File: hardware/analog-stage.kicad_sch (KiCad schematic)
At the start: 4 parts, among them U701 AD9834, U702 OPA695, U703 THS3491, U704 TS5A3159ADCK

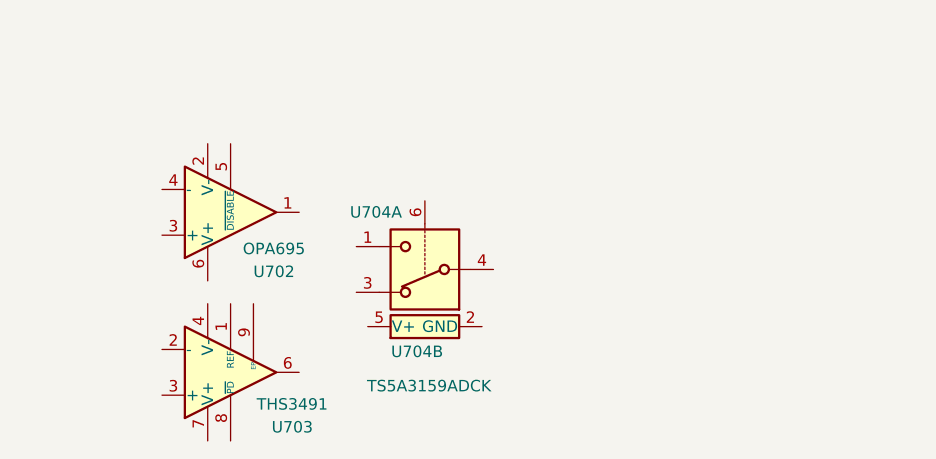
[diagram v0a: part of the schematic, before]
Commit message: Begin analog
Created LTspice simulation for square wave AC coupling.
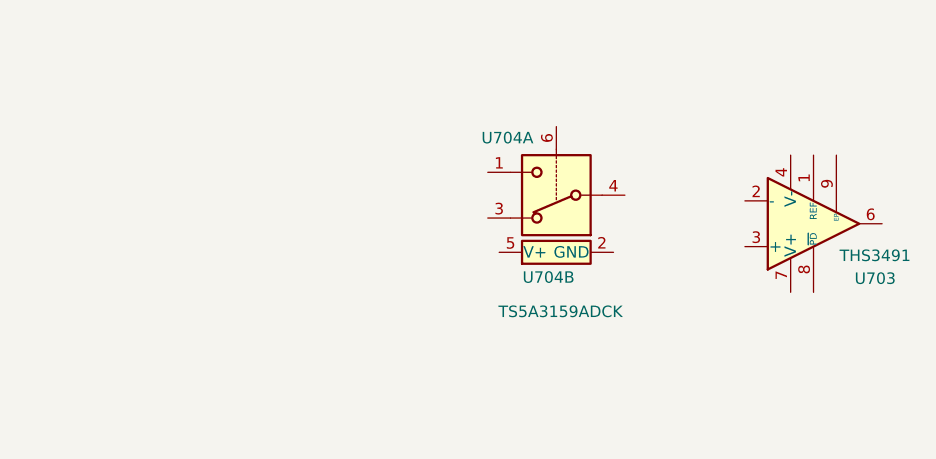
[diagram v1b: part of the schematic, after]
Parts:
- removed U702: OPA695, Package_TO_SOT_SMD:SOT-23-6, symbol carrier-wave:OPA695
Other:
- moved on the sheet: U703, U704A, U704B

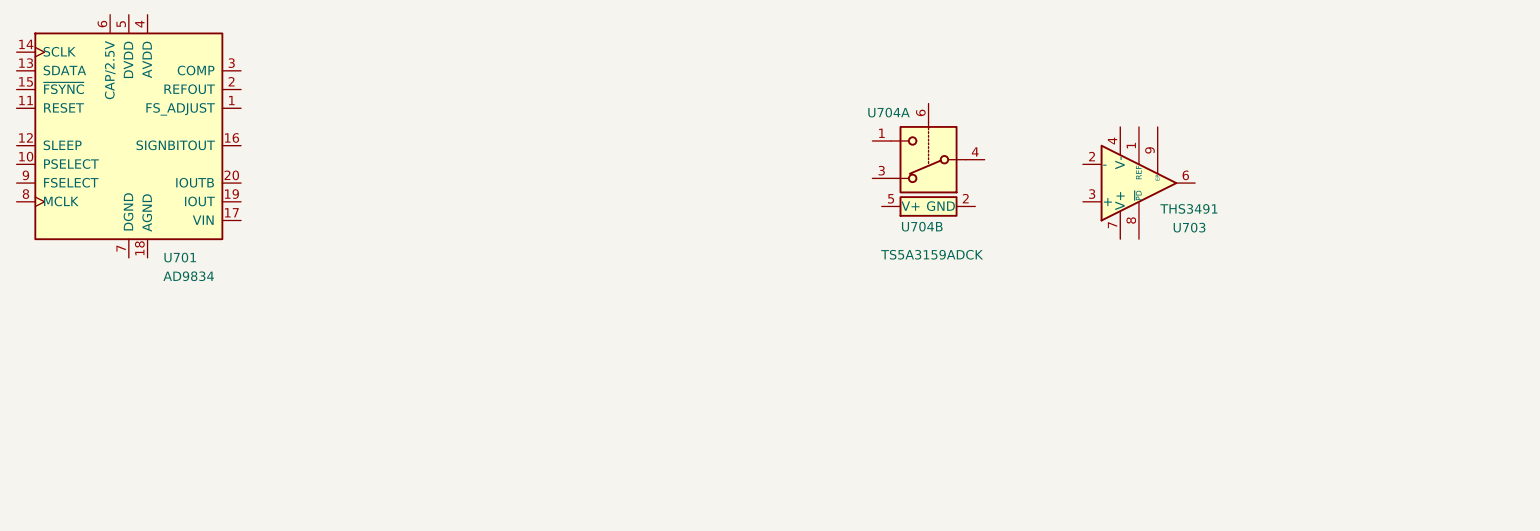
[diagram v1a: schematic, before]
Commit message: Place analog components
Proposed analog amp components in schematic
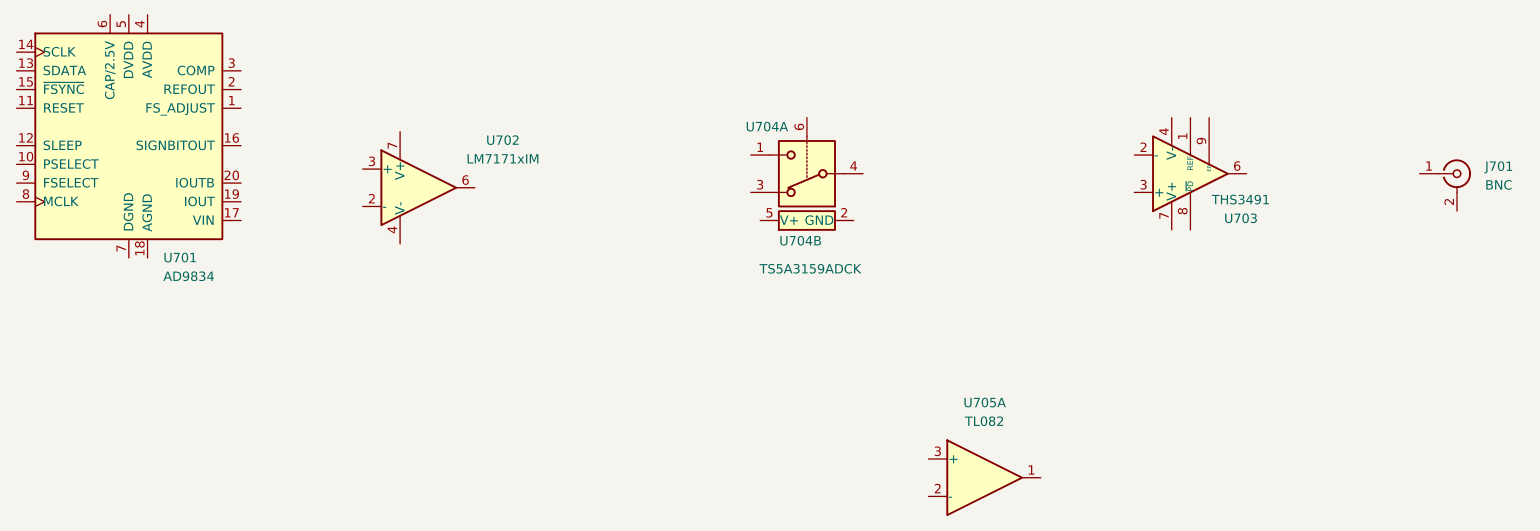
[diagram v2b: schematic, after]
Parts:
- added J701: BNC, symbol Connector:Conn_Coaxial
- added U702: LM7171xIM, Package_SO:SOIC-8_3.9x4.9mm_P1.27mm, symbol Amplifier_Operational:LM7171xIM
- added U705: TL082, Package_SO:SOIC-8_3.9x4.9mm_P1.27mm, symbol Amplifier_Operational:TL082
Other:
- moved on the sheet: U703, U704A, U704B

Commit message: Begin VGA impl
Sim and notes on adjusting to 4.5V rails for VGA.
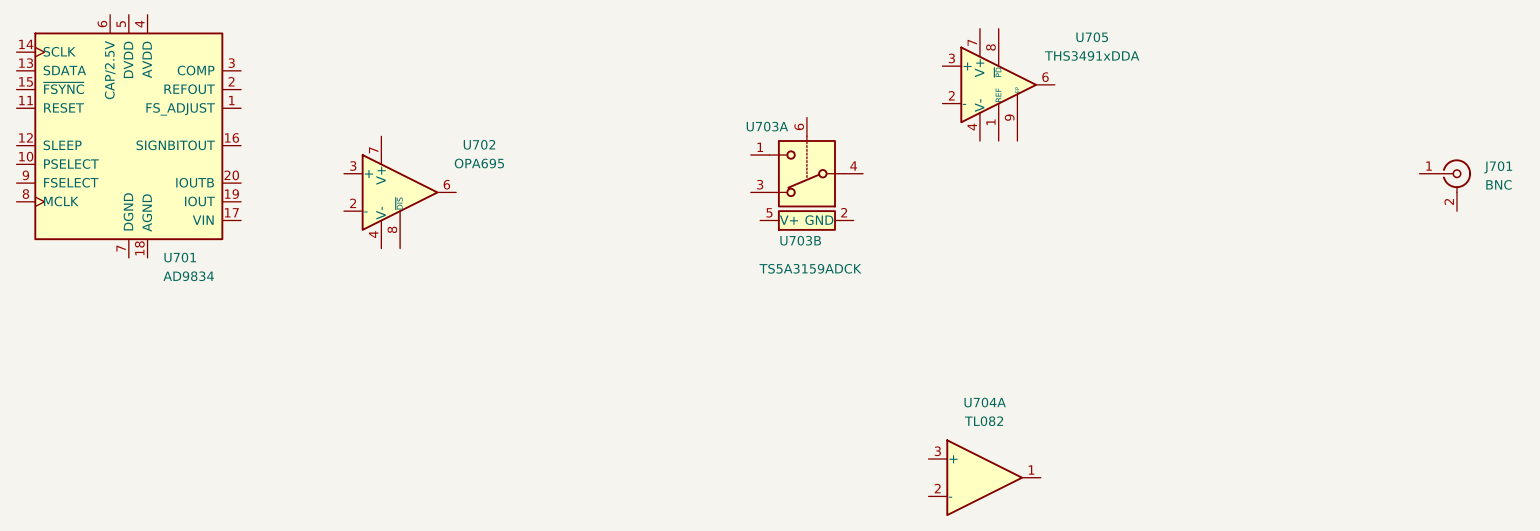
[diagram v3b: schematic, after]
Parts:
- removed U702: LM7171xIM, Package_SO:SOIC-8_3.9x4.9mm_P1.27mm, symbol Amplifier_Operational:LM7171xIM
- removed U703: THS3491, Package_SO:Texas_R-PDSO-G8_EP2.95x4.9mm_Mask2.4x3.1mm_ThermalVias, symbol Amplifier_Operational:THS3491xDDA
- added U702: OPA695, Package_SO:SOIC-8_3.9x4.9mm_P1.27mm, symbol carrier-wave:OPA695
- added U705: THS3491xDDA, Package_SO:Texas_R-PDSO-G8_EP2.95x4.9mm_Mask2.4x3.1mm_ThermalVias, symbol Amplifier_Operational:THS3491xDDA
- renumbered U704 to U703, U705 to U704
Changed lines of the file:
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@@
+	)
+	(symbol
+		(lib_id "carrier-wave:OPA695")
+		(at 97.79 97.79 0)
+		(unit 1)
+		(body_style 1)
+		(exclude_from_sim no)
+		(in_bom yes)
+		(on_board yes)
+		(in_pos_files yes)
+		(dnp no)
+		(fields_autoplaced yes)
+		(property "Reference" "U702"
+			(at 108.585 91.3698 0)
+			(show_name no)
+			(do_not_autoplace no)
+			(effects
+				(font
+					(size 1.27 1.27)
+				)
+			)
+		)
+		(property "Value" "OPA695"
+			(at 108.585 93.9098 0)
+			(show_name no)
+			(do_not_autoplace no)
+			(effects
+				(font
+					(size 1.27 1.27)
+				)
+			)
+		)
+		(property "Footprint" "Package_SO:SOIC-8_3.9x4.9mm_P1.27mm"
+			(at 100.33 104.14 0)
+			(hide yes)
+			(show_name no)
+			(do_not_autoplace no)
+			(effects
+				(font
+					(size 1.27 1.27)
+				)
+				(justify left)
+			)
+		)
+		(property "Datasheet" "https://www.ti.com/lit/ds/symlink/opa695.pdf"
+			(at 101.6 93.98 0)
+			(hide yes)
+			(show_name no)
+			(do_not_autoplace no)
+			(effects
+				(font
+					(size 1.27 1.27)
+				)
+			)
+		)
+		(property "Description" "Ultra-Wideband, Current-Feedback Operational Amplifier With Disable"
+			(at 97.79 97.79 0)
+			(hide yes)
+			(show_name no)
+			(do_not_autoplace no)
+			(effects
+				(font
+					(size 1.27 1.27)
+				)
+			)
+		)
+		(property "Part Number" " OPA695IDR"
+			(at 97.79 97.79 0)
+			(hide yes)
+			(show_name no)
+			(do_not_autoplace no)
+			(effects
+				(font
+					(size 1.27 1.27)
+				)
+			)
+		)
+		(property "Vendor URL" "https://www.digikey.com/en/products/detail/texas-instruments/OPA695IDR/1572891"
+			(at 97.79 97.79 0)
+			(hide yes)
+			(show_name no)
+			(do_not_autoplace no)
+			(effects
+				(font
+					(size 1.27 1.27)
+				)
+			)
+		)
+		(pin "5"
+		)
+		(pin "2"
+		)
+		(pin "1"
+		)
+		(pin "6"
+		)
+		(pin "4"
+		)
+		(pin "3"
+		)
+		(pin "8"
+		)
+		(pin "7"
+		)
+		(instances
+			(project "carrier-wave"
+				(path "/dc900721-a2e3-4f11-b4f2-59bb3a47422e/5675522c-b478-4fae-bc1e-6c223e44ab27"
+					(reference "U702")
+					(unit 1)
+				)
+			)
+		)
+	)
+	(symbol
+		(lib_id "Amplifier_Operational:THS3491xDDA")
+		(at 179.07 83.185 0)
+		(unit 1)
+		(body_style 1)
+		(exclude_from_sim no)
+		(in_bom yes)
+		(on_board yes)
+		(in_pos_files yes)
+		(dnp no)
+		(fields_autoplaced yes)
+		(property "Reference" "U705"
+			(at 191.77 76.7648 0)
+			(show_name no)
+			(do_not_autoplace no)
+			(effects
+				(font
+					(size 1.27 1.27)
+				)
+			)
+		)
+		(property "Value" "THS3491xDDA"
+			(at 191.77 79.3048 0)
+			(show_name no)
+			(do_not_autoplace no)
+			(effects
+				(font
+					(size 1.27 1.27)
+				)
+			)
+		)
+		(property "Footprint" "Package_SO:Texas_R-PDSO-G8_EP2.95x4.9mm_Mask2.4x3.1mm_ThermalVias"
+			(at 179.07 98.425 0)
+			(hide yes)
+			(show_name no)
+			(do_not_autoplace no)
+			(effects
+				(font
+					(size 1.27 1.27)
+				)
+			)
+		)
+		(property "Datasheet" "http://www.ti.com/lit/ds/symlink/ths3491.pdf"
+			(at 182.88 79.375 0)
+			(hide yes)
+			(show_name no)
+			(do_not_autoplace no)
+			(effects
+				(font
+					(size 1.27 1.27)
+				)
+			)
+		)
+		(property "Description" "900-MHz, 500-mA High-Power Output Current Feedback Operational Amplifier, SOIC-8"
+			(at 179.07 83.185 0)
+			(hide yes)
+			(show_name no)
+			(do_not_autoplace no)
+			(effects
+				(font
+					(size 1.27 1.27)
+				)
+			)
+		)
+		(pin "2"
+		)
+		(pin "5"
+		)
+		(pin "1"
+		)
+		(pin "6"
+		)
+		(pin "7"
+		)
+		(pin "8"
+		)
+		(pin "3"
+		)
+		(pin "9"
+		)
+		(pin "4"
+		)
+		(instances
+			(project "carrier-wave"
+				(path "/dc900721-a2e3-4f11-b4f2-59bb3a47422e/5675522c-b478-4fae-bc1e-6c223e44ab27"
+					(reference "U705")
+					(unit 1)
+				)
+			)
+		)
 	)
 	(symbol
@@
 		(in_pos_files yes)
 		(dnp no)
-		(property "Reference" "U704"
+		(property "Reference" "U703"
 			(at 150.495 88.9 0)
 			(show_name no)
@@
 			(project "carrier-wave"
 				(path "/dc900721-a2e3-4f11-b4f2-59bb3a47422e/5675522c-b478-4fae-bc1e-6c223e44ab27"
-					(reference "U704")
+					(reference "U703")
 					(unit 1)
 				)
@@
 		(dnp no)
 		(fields_autoplaced yes)
-		(property "Reference" "U705"
+		(property "Reference" "U704"
 			(at 177.165 126.365 0)
 			(show_name no)
@@
 		)
 		(property "Description" "Dual JFET-Input Operational Amplifiers, DIP-8/SOIC-8/SSOP-8"
+			(at 177.165 136.525 0)
+			(hide yes)
+			(show_name no)
+			(do_not_autoplace no)
+			(effects
+				(font
+					(size 1.27 1.27)
+				)
+			)
+		)
+		(property "Part Number" ""
+			(at 177.165 136.525 0)
+			(hide yes)
+			(show_name no)
+			(do_not_autoplace no)
+			(effects
+				(font
+					(size 1.27 1.27)
+				)
+			)
+		)
+		(property "Vendor URL" ""
 			(at 177.165 136.525 0)
 			(hide yes)
@@
 			(project "carrier-wave"
 				(path "/dc900721-a2e3-4f11-b4f2-59bb3a47422e/5675522c-b478-4fae-bc1e-6c223e44ab27"
-					(reference "U705")
-					(unit 1)
-				)
-			)
-		)
-	)
-	(symbol
-		(lib_id "Amplifier_Operational:THS3491xDDA")
-		(at 205.105 95.25 0)
-		(mirror x)
-		(unit 1)
-		(body_style 1)
-		(exclude_from_sim no)
-		(in_bom yes)
-		(on_board yes)
-		(in_pos_files yes)
-		(dnp no)
-		(property "Reference" "U703"
-			(at 211.963 101.346 0)
-			(show_name no)
-			(do_not_autoplace no)
-			(effects
-				(font
-					(size 1.27 1.27)
-				)
-			)
-		)
-		(property "Value" "THS3491"
-			(at 211.963 98.806 0)
-			(show_name no)
-			(do_not_autoplace no)
-			(effects
-				(font
-					(size 1.27 1.27)
-				)
-			)
-		)
-		(property "Footprint" "Package_SO:Texas_R-PDSO-G8_EP2.95x4.9mm_Mask2.4x3.1mm_ThermalVias"
-			(at 205.105 80.01 0)
-			(hide yes)
-			(show_name no)
-			(do_not_autoplace no)
-			(effects
-				(font
-					(size 1.27 1.27)
-				)
-			)
-		)
-		(property "Datasheet" "http://www.ti.com/lit/ds/symlink/ths3491.pdf"
-			(at 208.915 99.06 0)
-			(hide yes)
-			(show_name no)
-			(do_not_autoplace no)
-			(effects
-				(font
-					(size 1.27 1.27)
-				)
-			)
-		)
-		(property "Description" "900-MHz, 500-mA High-Power Output Current Feedback Operational Amplifier, SOIC-8"
-			(at 205.105 95.25 0)
-			(hide yes)
-			(show_name no)
-			(do_not_autoplace no)
-			(effects
-				(font
-					(size 1.27 1.27)
-				)
-			)
-		)
-		(pin "7"
-		)
-		(pin "4"
-		)
-		(pin "9"
-		)
-		(pin "8"
-		)
-		(pin "5"
-		)
-		(pin "2"
-		)
-		(pin "3"
-		)
-		(pin "6"
-		)
-		(pin "1"
-		)
-		(instances
-			(project "carrier-wave"
-				(path "/dc900721-a2e3-4f11-b4f2-59bb3a47422e/5675522c-b478-4fae-bc1e-6c223e44ab27"
-					(reference "U703")
+					(reference "U704")
 					(unit 1)
 				)
@@
 	)
 	(symbol
-		(lib_id "Amplifier_Operational:LM7171xIM")
-		(at 100.33 97.155 0)
-		(unit 1)
-		(body_style 1)
-		(exclude_from_sim no)
-		(in_bom yes)
-		(on_board yes)
-		(in_pos_files yes)
-		(dnp no)
-		(fields_autoplaced yes)
-		(property "Reference" "U702"
-			(at 111.76 90.7348 0)
-			(show_name no)
-			(do_not_autoplace no)
-			(effects
-				(font
-					(size 1.27 1.27)
-				)
-			)
-		)
-		(property "Value" "LM7171xIM"
-			(at 111.76 93.2748 0)
-			(show_name no)
-			(do_not_autoplace no)
-			(effects
-				(font
-					(size 1.27 1.27)
-				)
-			)
-		)
-		(property "Footprint" "Package_SO:SOIC-8_3.9x4.9mm_P1.27mm"
-			(at 100.33 97.155 0)
-			(hide yes)
-			(show_name no)
-			(do_not_autoplace no)
-			(effects
-				(font
-					(size 1.27 1.27)
-				)
-			)
-		)
-		(property "Datasheet" "https://www.ti.com/lit/ds/symlink/lm7171.pdf"
-			(at 100.33 97.155 0)
-			(hide yes)
-			(show_name no)
-			(do_not_autoplace no)
-			(effects
-				(font
-					(size 1.27 1.27)
-				)
-			)
-		)
-		(property "Description" "Single Very High Speed High Output Current Voltage Feedback Amplifier, SOIC-8"
-			(at 100.33 97.155 0)
-			(hide yes)
-			(show_name no)
-			(do_not_autoplace no)
-			(effects
-				(font
-					(size 1.27 1.27)
-				)
-			)
-		)
-		(pin "7"
-		)
-		(pin "2"
-		)
-		(pin "5"
-		)
-		(pin "8"
-		)
-		(pin "1"
-		)
-		(pin "4"
-		)
-		(pin "3"
-		)
-		(pin "6"
-		)
-		(instances
-			(project "carrier-wave"
-				(path "/dc900721-a2e3-4f11-b4f2-59bb3a47422e/5675522c-b478-4fae-bc1e-6c223e44ab27"
-					(reference "U702")
-					(unit 1)
-				)
-			)
-		)
-	)
-	(symbol
 		(lib_id "Analog_Switch:TS5A3159ADCK")
 		(at 153.035 101.6 90)
@@
 		(in_pos_files yes)
 		(dnp no)
-		(property "Reference" "U704"
+		(property "Reference" "U703"
 			(at 155.067 104.394 90)
 			(show_name no)
@@
 			(project "carrier-wave"
 				(path "/dc900721-a2e3-4f11-b4f2-59bb3a47422e/5675522c-b478-4fae-bc1e-6c223e44ab27"
-					(reference "U704")
+					(reference "U703")
 					(unit 2)
 				)
